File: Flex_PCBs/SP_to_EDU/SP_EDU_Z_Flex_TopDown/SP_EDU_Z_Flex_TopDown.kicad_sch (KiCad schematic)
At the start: 2 parts, among them J1 Conn_01x08_Male, J2 Conn_01x08_Male

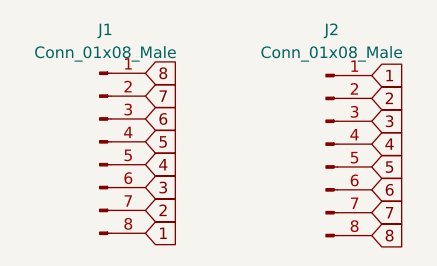
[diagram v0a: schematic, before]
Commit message: replace ZF5S-*-01-T-WT and 2005280040 connectors with T1M-*-F-SH-L-FR connector
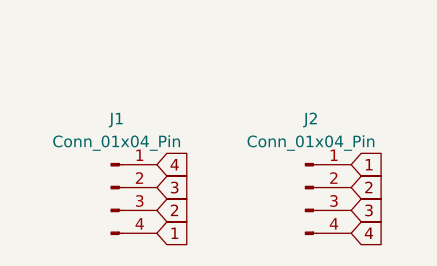
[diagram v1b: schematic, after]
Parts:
- removed J1, J2: Conn_01x08_Male, STS_connector:flexpcb con., symbol Connector:Conn_01x08_Male
- added J1, J2: Conn_01x04_Pin, STS_connector:flexPCB_connector_edu_sensors_new, symbol Connector:Conn_01x04_Pin
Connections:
- net 1: now also J1.4 (Pin_4), J2.1 (Pin_1)
- net 2: now also J1.3 (Pin_3), J2.2 (Pin_2)
- net 3: now also J1.2 (Pin_2), J2.3 (Pin_3)
- net 4: now also J1.1 (Pin_1), J2.4 (Pin_4)
